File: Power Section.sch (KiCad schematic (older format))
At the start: 20 parts, among them J1 BATT, Q1 IRLML9301TRPBF, SW5 SW_SPDT, U1 LM1117LDX, U2 LM1117LDX, U3 LM1117LDX

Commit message: Major upgrade
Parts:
- removed SW5: SW_SPDT, Connector_PinHeader_2.54mm:PinHeader_2x03_P2.54mm_Vertical_SMD, symbol Switch:SW_SPDT
- added J17: Conn_01x03, Button_Switch_SMD:SW_SPDT_CK-JS102011SAQN, symbol Connector_Generic:Conn_01x03
- J1: footprint (none) -> Connector_PinHeader_2.54mm:PinHeader_1x02_P2.54mm_Vertical
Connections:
- wire segments 69 -> 71
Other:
- moved on the sheet: J1
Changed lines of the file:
@@
 L Connector_Generic:Conn_01x02 J1
 U 1 1 5E80D37A
-P 1950 2800
-F 0 "J1" H 1868 3017 50  0000 C CNN
-F 1 "BATT" H 1868 2926 50  0000 C CNN
-F 2 "" H 1950 2800 50  0001 C CNN
-F 3 "~" H 1950 2800 50  0001 C CNN
-	1    1950 2800
+P 1950 2700
+F 0 "J1" H 1868 2917 50  0000 C CNN
+F 1 "BATT" H 1868 2826 50  0000 C CNN
+F 2 "Connector_PinHeader_2.54mm:PinHeader_1x02_P2.54mm_Vertical" H 1950 2700 50  0001 C CNN
+F 3 "~" H 1950 2700 50  0001 C CNN
+	1    1950 2700
 	-1   0    0    -1
 $EndComp
 Wire Wire Line
-	2150 2900 2250 2900
-Wire Wire Line
-	2250 2900 2250 3100
+	2150 2800 2250 2800
+Wire Wire Line
+	2250 2800 2250 3100
 Wire Wire Line
 	3800 2900 4200 2900
@@
 	3800 2700 4300 2700
 Wire Wire Line
-	2950 2700 3350 2700
-Wire Wire Line
 	4200 2900 4200 3250
 Wire Wire Line
@@
 Text Label 4000 2700 0    50   ~ 0
 VCC
-$Comp
-L Switch:SW_SPDT SW5
-U 1 1 5E70C14B
-P 2750 2800
-F 0 "SW5" H 2750 3085 50  0000 C CNN
-F 1 "SW_SPDT" H 2750 2994 50  0000 C CNN
-F 2 "Connector_PinHeader_2.54mm:PinHeader_2x03_P2.54mm_Vertical_SMD" H 2750 2800 50  0001 C CNN
-F 3 "~" H 2750 2800 50  0001 C CNN
-	1    2750 2800
-	1    0    0    -1
-$EndComp
-Wire Wire Line
-	2550 2800 2150 2800
+Wire Wire Line
+	2750 2700 2750 2500
+Wire Wire Line
+	2750 2700 3350 2700
+Wire Wire Line
+	2650 2700 2150 2700
+Wire Wire Line
+	2650 2500 2650 2700
+$Comp
+L Connector_Generic:Conn_01x03 J17
+U 1 1 5E785057
+P 2650 2300
+F 0 "J17" V 2614 2112 50  0000 R CNN
+F 1 "Conn_01x03" V 2523 2112 50  0000 R CNN
+F 2 "Button_Switch_SMD:SW_SPDT_CK-JS102011SAQN" H 2650 2300 50  0001 C CNN
+F 3 "~" H 2650 2300 50  0001 C CNN
+	1    2650 2300
+	0    -1   -1   0
+$EndComp
 $EndSCHEMATC

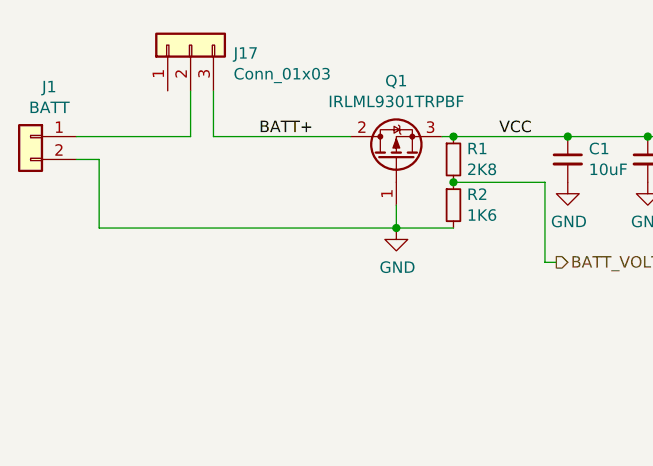
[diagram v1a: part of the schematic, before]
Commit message: Power on led
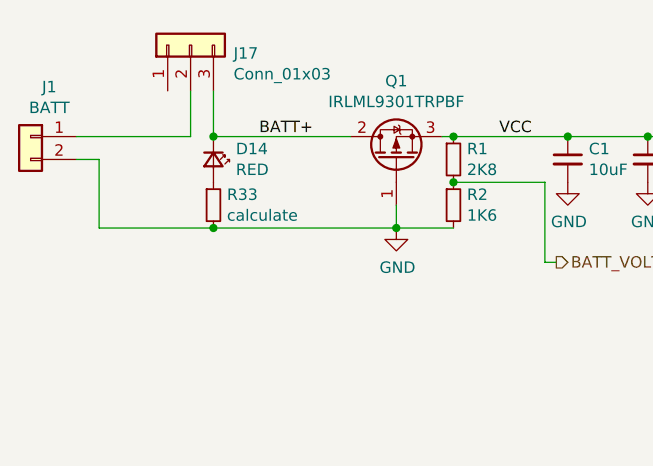
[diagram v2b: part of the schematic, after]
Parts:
- added D14: RED, LED_SMD:LED_0402_1005Metric, symbol Device:LED_Small
- added R33: calculate, Resistor_SMD:R_0402_1005Metric, symbol Device:R_Small
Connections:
- net BATT+: now also D14.1 (K)
- net GND: now also R33.2
- new net: D14.2 (A), R33.1
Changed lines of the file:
@@
 	3550 3100 3550 3000
 Wire Wire Line
-	3550 3100 2250 3100
+	3550 3100 2750 3100
 Connection ~ 3550 3100
 $Comp
@@
 	0    -1   -1   0
 $EndComp
+$Comp
+L Device:LED_Small D14
+U 1 1 5E6EB1F4
+P 2750 2800
+F 0 "D14" V 2704 2898 50  0000 L CNN
+F 1 "RED" V 2795 2898 50  0000 L CNN
+F 2 "LED_SMD:LED_0402_1005Metric" V 2750 2800 50  0001 C CNN
+F 3 "~" V 2750 2800 50  0001 C CNN
+	1    2750 2800
+	0    1    1    0
+$EndComp
+Connection ~ 2750 2700
+$Comp
+L Device:R_Small R33
+U 1 1 5E6EC105
+P 2750 3000
+F 0 "R33" H 2809 3046 50  0000 L CNN
+F 1 "calculate" H 2809 2955 50  0000 L CNN
+F 2 "Resistor_SMD:R_0402_1005Metric" H 2750 3000 50  0001 C CNN
+F 3 "~" H 2750 3000 50  0001 C CNN
+	1    2750 3000
+	1    0    0    -1
+$EndComp
+Connection ~ 2750 3100
+Wire Wire Line
+	2750 3100 2250 3100
 $EndSCHEMATC

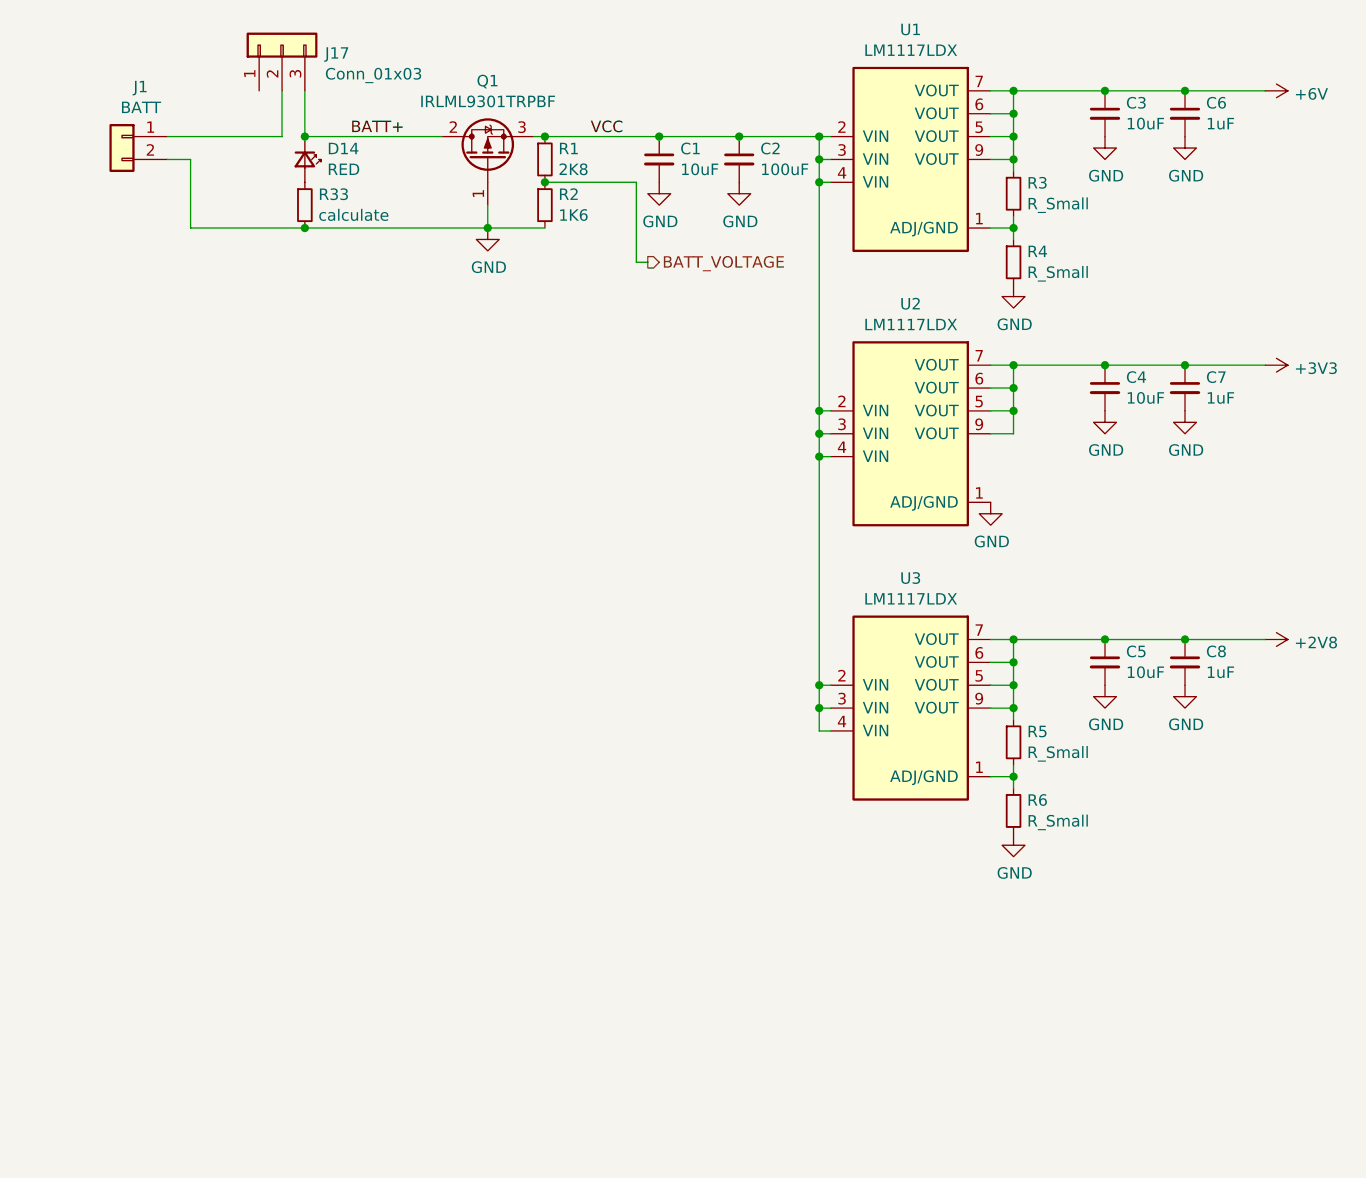
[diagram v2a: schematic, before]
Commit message: Added 5v rail
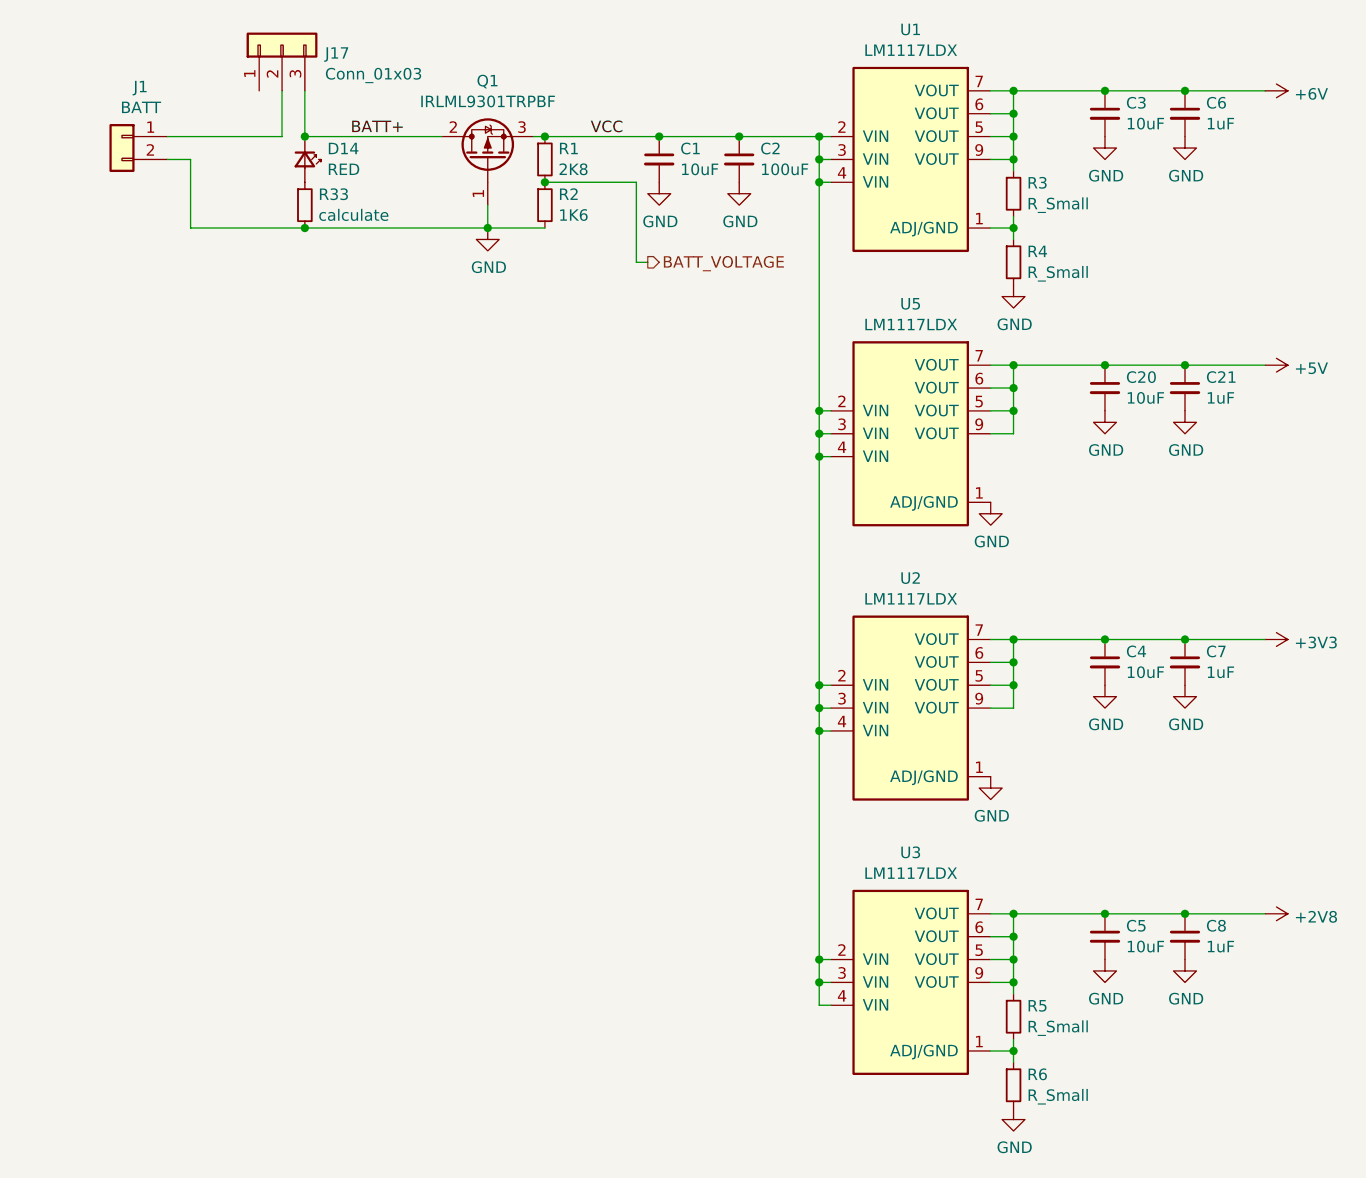
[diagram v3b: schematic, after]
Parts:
- added C20: 10uF, Capacitor_SMD:C_0603_1608Metric, symbol Device:C_Small
- added C21: 1uF, Capacitor_SMD:C_0402_1005Metric, symbol Device:C_Small
- added U5: LM1117LDX, Package_SON:WSON-8_4x4mm_P0.8mm, symbol LM1117:LM1117LDX
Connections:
- net GND: now also C20.2, C21.2, U5.1 (ADJ/GND)
- net VCC: now also U5.2 (VIN), U5.3 (VIN), U5.4 (VIN)
- new net +5V: C20.1, C21.1, U5.5 (VOUT), U5.6 (VOUT), U5.7 (VOUT), U5.9 (VOUT)
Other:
- moved on the sheet: C4, C5, C7, C8, R5, R6, U2, U3

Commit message: Changes in graphics, tweaks in power input, resistor values
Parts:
- removed Q1: IRLML9301TRPBF, Package_TO_SOT_SMD:SOT-23, symbol Device:Q_PMOS_GDS
- added Q1, Q7: IRLML9301TRPBF, Package_TO_SOT_SMD:SOT-23, symbol Device:Q_PMOS_GSD
- added R51, R52: 100K, Resistor_SMD:R_0402_1005Metric, symbol Device:R_Small
- added R53: 866R, Resistor_SMD:R_0402_1005Metric, symbol Device:R_Small
- added R54: 2K49, Resistor_SMD:R_0402_1005Metric, symbol Device:R_Small
- D14: value RED -> RED, 5mA
- R3: value R_Small -> 866R
- R33: value calculate -> 1.3K
- R4: value R_Small -> 3K16
- R5: value R_Small -> 620R
- R6: value R_Small -> 750R
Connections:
- net +5V: now also R53.1
- net BATT+: now also J1.1 (Pin_1), Q1.3 (D); no longer D14.1 (K), J17.3 (Pin_3)
- net GND: now also J17.3 (Pin_3), R54.2; no longer U5.1 (ADJ/GND)
- net VCC: now also D14.1 (K), Q7.3 (D)
- net at J17.2 (Pin_2): now also R51.1, R52.1; no longer J1.1 (Pin_1)
- new net: Q1.1 (G), Q7.1 (G), R52.2
- new net: Q1.2 (S), Q7.2 (S), R51.2
- new net: R53.2, R54.1, U5.1 (ADJ/GND)
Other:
- moved on the sheet: D14, J1, J17, R33
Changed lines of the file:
@@
 P 5850 2950
 F 0 "R3" H 5909 2996 50  0000 L CNN
-F 1 "R_Small" H 5909 2905 50  0000 L CNN
+F 1 "866R" H 5909 2905 50  0000 L CNN
 F 2 "Resistor_SMD:R_0402_1005Metric" H 5850 2950 50  0001 C CNN
 F 3 "~" H 5850 2950 50  0001 C CNN
@@
 P 5850 3250
 F 0 "R4" H 5909 3296 50  0000 L CNN
-F 1 "R_Small" H 5909 3205 50  0000 L CNN
+F 1 "3K16" H 5909 3205 50  0000 L CNN
 F 2 "Resistor_SMD:R_0402_1005Metric" H 5850 3250 50  0001 C CNN
 F 3 "~" H 5850 3250 50  0001 C CNN
@@
 Wire Wire Line
 	5850 2700 5850 2600
-$Comp
-L Device:Q_PMOS_GDS Q1
-U 1 1 5E809729
-P 3550 2800
-F 0 "Q1" V 3893 2800 50  0000 C CNN
-F 1 "IRLML9301TRPBF" V 3802 2800 50  0000 C CNN
-F 2 "Package_TO_SOT_SMD:SOT-23" H 3750 2900 50  0001 C CNN
-F 3 "~" H 3550 2800 50  0001 C CNN
-	1    3550 2800
-	0    -1   -1   0
-$EndComp
-Wire Wire Line
-	3750 2700 3800 2700
 Wire Wire Line
 	5000 2700 5000 2800
@@
 	1    0    0    -1
 $EndComp
-Wire Wire Line
-	3800 3100 3550 3100
-Wire Wire Line
-	3550 3100 3550 3000
-Wire Wire Line
-	3550 3100 2750 3100
-Connection ~ 3550 3100
 $Comp
 L Connector_Generic:Conn_01x02 J1
 U 1 1 5E80D37A
-P 1950 2700
-F 0 "J1" H 1868 2917 50  0000 C CNN
-F 1 "BATT" H 1868 2826 50  0000 C CNN
-F 2 "Connector_PinHeader_2.54mm:PinHeader_1x02_P2.54mm_Vertical" H 1950 2700 50  0001 C CNN
-F 3 "~" H 1950 2700 50  0001 C CNN
-	1    1950 2700
+P 1550 2700
+F 0 "J1" H 1468 2917 50  0000 C CNN
+F 1 "BATT" H 1468 2826 50  0000 C CNN
+F 2 "Connector_PinHeader_2.54mm:PinHeader_1x02_P2.54mm_Vertical" H 1550 2700 50  0001 C CNN
+F 3 "~" H 1550 2700 50  0001 C CNN
+	1    1550 2700
 	-1   0    0    -1
 $EndComp
 Wire Wire Line
-	2150 2800 2250 2800
-Wire Wire Line
-	2250 2800 2250 3100
+	1750 2800 1900 2800
 Wire Wire Line
 	3800 2900 4200 2900
@@
 P 5850 6550
 F 0 "R5" H 5909 6596 50  0000 L CNN
-F 1 "R_Small" H 5909 6505 50  0000 L CNN
+F 1 "620R" H 5909 6505 50  0000 L CNN
 F 2 "Resistor_SMD:R_0402_1005Metric" H 5850 6550 50  0001 C CNN
 F 3 "~" H 5850 6550 50  0001 C CNN
@@
 P 5850 6850
 F 0 "R6" H 5909 6896 50  0000 L CNN
-F 1 "R_Small" H 5909 6805 50  0000 L CNN
+F 1 "750R" H 5909 6805 50  0000 L CNN
 F 2 "Resistor_SMD:R_0402_1005Metric" H 5850 6850 50  0001 C CNN
 F 3 "~" H 5850 6850 50  0001 C CNN
@@
 L power:GND #PWR0195
 U 1 1 5E892532
-P 3550 3100
-F 0 "#PWR0195" H 3550 2850 50  0001 C CNN
-F 1 "GND" H 3555 2927 50  0000 C CNN
-F 2 "" H 3550 3100 50  0001 C CNN
-F 3 "" H 3550 3100 50  0001 C CNN
-	1    3550 3100
-	1    0    0    -1
-$EndComp
-Text Label 2950 2700 0    50   ~ 0
+P 1900 3550
+F 0 "#PWR0195" H 1900 3300 50  0001 C CNN
+F 1 "GND" H 1905 3377 50  0000 C CNN
+F 2 "" H 1900 3550 50  0001 C CNN
+F 3 "" H 1900 3550 50  0001 C CNN
+	1    1900 3550
+	1    0    0    -1
+$EndComp
+Text Label 1800 2700 0    50   ~ 0
 BATT+
 Text Label 4000 2700 0    50   ~ 0
 VCC
-Wire Wire Line
-	2750 2700 2750 2500
-Wire Wire Line
-	2750 2700 3350 2700
-Wire Wire Line
-	2650 2700 2150 2700
-Wire Wire Line
-	2650 2500 2650 2700
 $Comp
 L Connector_Generic:Conn_01x03 J17
 U 1 1 5E785057
-P 2650 2300
-F 0 "J17" V 2614 2112 50  0000 R CNN
-F 1 "Conn_01x03" V 2523 2112 50  0000 R CNN
-F 2 "Button_Switch_SMD:SW_SPDT_CK-JS102011SAQN" H 2650 2300 50  0001 C CNN
-F 3 "~" H 2650 2300 50  0001 C CNN
-	1    2650 2300
-	0    -1   -1   0
+P 3250 3300
+F 0 "J17" V 3450 3450 50  0000 R CNN
+F 1 "Conn_01x03" V 3350 3600 50  0000 R CNN
+F 2 "Button_Switch_SMD:SW_SPDT_CK-JS102011SAQN" H 3250 3300 50  0001 C CNN
+F 3 "~" H 3250 3300 50  0001 C CNN
+	1    3250 3300
+	1    0    0    -1
 $EndComp
 $Comp
 L Device:LED_Small D14
 U 1 1 5E6EB1F4
-P 2750 2800
-F 0 "D14" V 2704 2898 50  0000 L CNN
-F 1 "RED" V 2795 2898 50  0000 L CNN
-F 2 "LED_SMD:LED_0402_1005Metric" V 2750 2800 50  0001 C CNN
-F 3 "~" V 2750 2800 50  0001 C CNN
-	1    2750 2800
+P 3550 3250
+F 0 "D14" V 3504 3348 50  0000 L CNN
+F 1 "RED, 5mA" V 3595 3348 50  0000 L CNN
+F 2 "LED_SMD:LED_0402_1005Metric" V 3550 3250 50  0001 C CNN
+F 3 "~" V 3550 3250 50  0001 C CNN
+	1    3550 3250
 	0    1    1    0
 $EndComp
-Connection ~ 2750 2700
 $Comp
 L Device:R_Small R33
 U 1 1 5E6EC105
-P 2750 3000
-F 0 "R33" H 2809 3046 50  0000 L CNN
-F 1 "calculate" H 2809 2955 50  0000 L CNN
-F 2 "Resistor_SMD:R_0402_1005Metric" H 2750 3000 50  0001 C CNN
-F 3 "~" H 2750 3000 50  0001 C CNN
-	1    2750 3000
-	1    0    0    -1
-$EndComp
-Connection ~ 2750 3100
-Wire Wire Line
-	2750 3100 2250 3100
+P 3550 3450
+F 0 "R33" H 3609 3496 50  0000 L CNN
+F 1 "1.3K" H 3609 3405 50  0000 L CNN
+F 2 "Resistor_SMD:R_0402_1005Metric" H 3550 3450 50  0001 C CNN
+F 3 "~" H 3550 3450 50  0001 C CNN
+	1    3550 3450
+	1    0    0    -1
+$EndComp
 $Comp
 L LM1117:LM1117LDX U5
@@
 Wire Wire Line
 	6600 3700 6950 3700
-$Comp
-L power:GND #PWR0161
-U 1 1 5E71ECC4
-P 5750 4300
-F 0 "#PWR0161" H 5750 4050 50  0001 C CNN
-F 1 "GND" H 5755 4127 50  0000 C CNN
-F 2 "" H 5750 4300 50  0001 C CNN
-F 3 "" H 5750 4300 50  0001 C CNN
-	1    5750 4300
-	1    0    0    -1
-$EndComp
 Wire Wire Line
 	5050 6500 5000 6500
@@
 	0    1    1    0
 $EndComp
+$Comp
+L Device:R_Small R52
+U 1 1 5E6498EA
+P 2850 3150
+F 0 "R52" H 2909 3196 50  0000 L CNN
+F 1 "100K" H 2909 3105 50  0000 L CNN
+F 2 "Resistor_SMD:R_0402_1005Metric" H 2850 3150 50  0001 C CNN
+F 3 "~" H 2850 3150 50  0001 C CNN
+	1    2850 3150
+	1    0    0    1
+$EndComp
+Wire Wire Line
+	2100 2700 1750 2700
+$Comp
+L Device:R_Small R51
+U 1 1 5E671F2F
+P 2550 3150
+F 0 "R51" H 2609 3196 50  0000 L CNN
+F 1 "100K" H 2609 3105 50  0000 L CNN
+F 2 "Resistor_SMD:R_0402_1005Metric" H 2550 3150 50  0001 C CNN
+F 3 "~" H 2550 3150 50  0001 C CNN
+	1    2550 3150
+	1    0    0    1
+$EndComp
+Wire Wire Line
+	1900 2800 1900 3550
+Wire Wire Line
+	3800 3100 3800 3550
+Connection ~ 1900 3550
+Wire Wire Line
+	3050 3400 3050 3550
+Wire Wire Line
+	3050 3550 3550 3550
+Wire Wire Line
+	1900 3550 3050 3550
+Connection ~ 3050 3550
+Wire Wire Line
+	3350 2700 3550 2700
+Wire Wire Line
+	2500 2700 2550 2700
+Connection ~ 2550 2700
+Wire Wire Line
+	2550 2700 2950 2700
+Wire Wire Line
+	2550 2700 2550 3050
+Wire Wire Line
+	2300 3000 2850 3000
+Connection ~ 2850 3000
+Wire Wire Line
+	2850 3000 3150 3000
+Wire Wire Line
+	3050 3300 2850 3300
+Connection ~ 2850 3300
+Wire Wire Line
+	2850 3300 2550 3300
+Wire Wire Line
+	2850 3050 2850 3000
+Wire Wire Line
+	2850 3300 2850 3250
+Wire Wire Line
+	2550 3300 2550 3250
+Connection ~ 3550 3550
+Wire Wire Line
+	3550 3550 3800 3550
+Wire Wire Line
+	3550 3150 3550 2700
+Connection ~ 3550 2700
+Wire Wire Line
+	3550 2700 3800 2700
+$Comp
+L Device:Q_PMOS_GSD Q1
+U 1 1 5E759320
+P 2300 2800
+F 0 "Q1" V 2643 2800 50  0000 C CNN
+F 1 "IRLML9301TRPBF" V 2552 2800 50  0000 C CNN
+F 2 "Package_TO_SOT_SMD:SOT-23" H 2500 2900 50  0001 C CNN
+F 3 "~" H 2300 2800 50  0001 C CNN
+	1    2300 2800
+	0    -1   -1   0
+$EndComp
+$Comp
+L Device:Q_PMOS_GSD Q7
+U 1 1 5E76404F
+P 3150 2800
+F 0 "Q7" V 3493 2800 50  0000 C CNN
+F 1 "IRLML9301TRPBF" V 3402 2800 50  0000 C CNN
+F 2 "Package_TO_SOT_SMD:SOT-23" H 3350 2900 50  0001 C CNN
+F 3 "~" H 3150 2800 50  0001 C CNN
+	1    3150 2800
+	0    1    -1   0
+$EndComp
+$Comp
+L Device:R_Small R53
+U 1 1 5E786A47
+P 5850 4150
+F 0 "R53" H 5909 4196 50  0000 L CNN
+F 1 "866R" H 5909 4105 50  0000 L CNN
+F 2 "Resistor_SMD:R_0402_1005Metric" H 5850 4150 50  0001 C CNN
+F 3 "~" H 5850 4150 50  0001 C CNN
+	1    5850 4150
+	1    0    0    -1
+$EndComp
+$Comp
+L Device:R_Small R54
+U 1 1 5E786A4D
+P 5850 4450
+F 0 "R54" H 5909 4496 50  0000 L CNN
+F 1 "2K49" H 5909 4405 50  0000 L CNN
+F 2 "Resistor_SMD:R_0402_1005Metric" H 5850 4450 50  0001 C CNN
+F 3 "~" H 5850 4450 50  0001 C CNN
+	1    5850 4450
+	1    0    0    -1
+$EndComp
+Wire Wire Line
+	5750 4300 5850 4300
+Wire Wire Line
+	5850 4300 5850 4250
+Wire Wire Line
+	5850 4300 5850 4350
+Connection ~ 5850 4300
+$Comp
+L power:GND #PWR0161
+U 1 1 5E786A57
+P 5850 4550
+F 0 "#PWR0161" H 5850 4300 50  0001 C CNN
+F 1 "GND" H 5855 4377 50  0000 C CNN
+F 2 "" H 5850 4550 50  0001 C CNN
+F 3 "" H 5850 4550 50  0001 C CNN
+	1    5850 4550
+	1    0    0    -1
+$EndComp
+Wire Wire Line
+	5850 4050 5850 4000
+Connection ~ 5850 4000
 $EndSCHEMATC

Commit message: Issues
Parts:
- added C?: 100uF, Capacitor_SMD:C_0805_2012Metric, symbol Device:C_Small
- R4: value 3K16 -> 3K32
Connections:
- net +6V: now also C?.1
- net GND: now also C?.2
- net VCC: now also D14.2 (A); no longer D14.1 (K)
- net at R33.1: now also D14.1 (K); no longer D14.2 (A)
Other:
- moved on the sheet: D14
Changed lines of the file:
@@
 P 5850 3250
 F 0 "R4" H 5909 3296 50  0000 L CNN
-F 1 "3K16" H 5909 3205 50  0000 L CNN
+F 1 "3K32" H 5909 3205 50  0000 L CNN
 F 2 "Resistor_SMD:R_0402_1005Metric" H 5850 3250 50  0001 C CNN
 F 3 "~" H 5850 3250 50  0001 C CNN
@@
 Connection ~ 6250 2500
 Wire Wire Line
-	6600 2500 6950 2500
+	6600 2500 6900 2500
 Connection ~ 6600 2500
 $Comp
@@
 U 1 1 5E6EB1F4
 P 3550 3250
-F 0 "D14" V 3504 3348 50  0000 L CNN
-F 1 "RED, 5mA" V 3595 3348 50  0000 L CNN
+F 0 "D14" V 3600 3000 50  0000 L CNN
+F 1 "RED, 5mA" V 3500 2800 50  0000 L CNN
 F 2 "LED_SMD:LED_0402_1005Metric" V 3550 3250 50  0001 C CNN
 F 3 "~" V 3550 3250 50  0001 C CNN
 	1    3550 3250
-	0    1    1    0
+	0    -1   -1   0
 $EndComp
 $Comp
@@
 	5850 4050 5850 4000
 Connection ~ 5850 4000
+$Comp
+L Device:C_Small C?
+U 1 1 5E6588DD
+P 6900 2600
+F 0 "C?" H 6992 2646 50  0000 L CNN
+F 1 "100uF" H 6992 2555 50  0000 L CNN
+F 2 "Capacitor_SMD:C_0805_2012Metric" H 6900 2600 50  0001 C CNN
+F 3 "~" H 6900 2600 50  0001 C CNN
+	1    6900 2600
+	1    0    0    -1
+$EndComp
+Connection ~ 6900 2500
+Wire Wire Line
+	6900 2500 6950 2500
+$Comp
+L power:GND #PWR?
+U 1 1 5E658F51
+P 6900 2700
+F 0 "#PWR?" H 6900 2450 50  0001 C CNN
+F 1 "GND" H 6905 2527 50  0000 C CNN
+F 2 "" H 6900 2700 50  0001 C CNN
+F 3 "" H 6900 2700 50  0001 C CNN
+	1    6900 2700
+	1    0    0    -1
+$EndComp
 $EndSCHEMATC
